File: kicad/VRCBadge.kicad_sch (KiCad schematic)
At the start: 34 parts, among them J4 Conn_01x02, J5 USB_C_Receptacle_USB2.0_16P, J6 Conn_01x13_Socket, Q2 FS8205A, SW3 RESET, SW4 BOOT, U10 MAX17048G+T10, U6 DW01A, U7 ME6211C33M5, U8 TP4056-42-ESOP8, U9 ESP32-S3-WROOM-1U

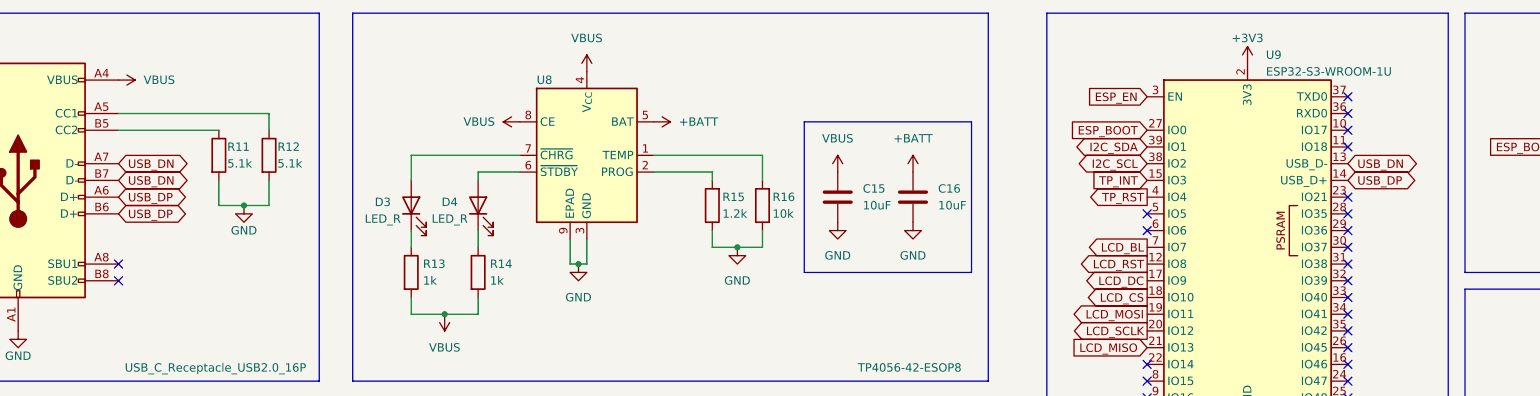
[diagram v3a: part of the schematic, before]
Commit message: chore: change usb data line global label and update footprint to 0402_1005
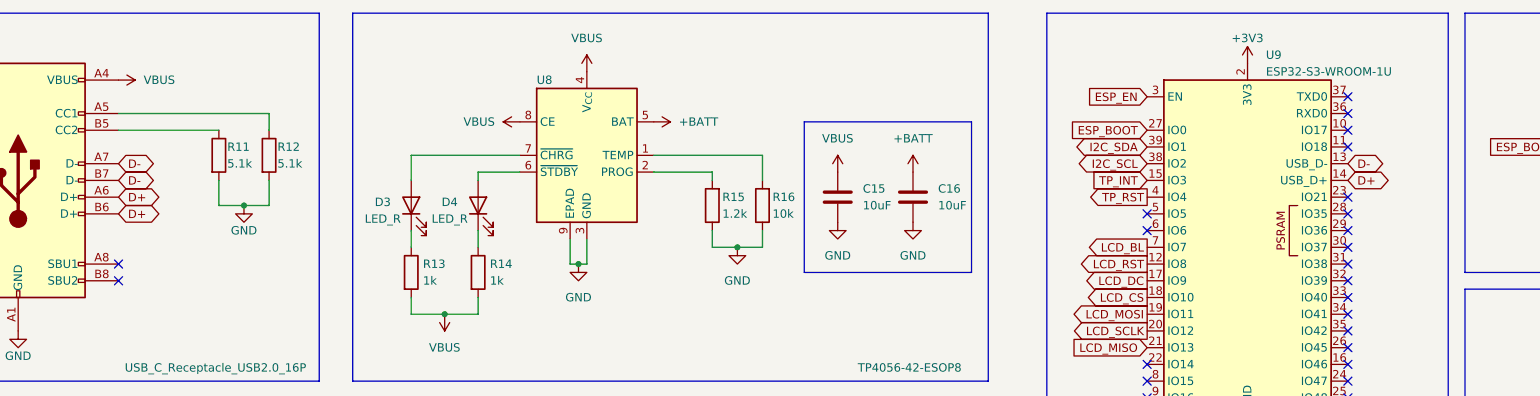
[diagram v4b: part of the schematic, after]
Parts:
- C12, C13, C14, C17, C19, C20, C21, C22: footprint Capacitor_SMD:C_0603_1608Metric -> Capacitor_SMD:C_0402_1005Metric
- C15, C16, C18: footprint Capacitor_SMD:C_0805_2012Metric -> Capacitor_SMD:C_0402_1005Metric
- D3, D4: footprint LED_SMD:LED_0603_1608Metric -> LED_SMD:LED_0402_1005Metric
- R11, R12, R13, R14, R15, R16, R17, R18, R19, R20: footprint Resistor_SMD:R_0603_1608Metric -> Resistor_SMD:R_0402_1005Metric
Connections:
- net USB_DN renamed D-
- net USB_DP renamed D+
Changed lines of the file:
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@@
 		)
 	)
-	(global_label "USB_DP"
+	(global_label "D+"
 		(shape bidirectional)
 		(at 50.8 48.26 0)
@@
 		)
 		(property "Intersheetrefs" "${INTERSHEET_REFS}"
-			(at 62.2141 48.26 0)
+			(at 57.7389 48.26 0)
 			(effects
 				(font
@@
 		)
 	)
-	(global_label "USB_DP"
+	(global_label "D+"
 		(shape bidirectional)
 		(at 50.8 50.8 0)
@@
 		)
 		(property "Intersheetrefs" "${INTERSHEET_REFS}"
-			(at 62.2141 50.8 0)
+			(at 57.7389 50.8 0)
 			(effects
 				(font
@@
 		)
 	)
-	(global_label "USB_DN"
+	(global_label "D-"
 		(shape bidirectional)
 		(at 50.8 43.18 0)
@@
 		)
 		(property "Intersheetrefs" "${INTERSHEET_REFS}"
-			(at 62.2746 43.18 0)
+			(at 57.7389 43.18 0)
 			(effects
 				(font
@@
 		)
 	)
-	(global_label "USB_DN"
+	(global_label "D-"
 		(shape bidirectional)
 		(at 237.49 43.18 0)
@@
 		)
 		(property "Intersheetrefs" "${INTERSHEET_REFS}"
-			(at 248.9646 43.18 0)
+			(at 244.4289 43.18 0)
 			(effects
 				(font
@@
 		)
 	)
-	(global_label "USB_DP"
+	(global_label "D+"
 		(shape bidirectional)
 		(at 237.49 45.72 0)
@@
 		)
 		(property "Intersheetrefs" "${INTERSHEET_REFS}"
-			(at 248.9041 45.72 0)
+			(at 244.4289 45.72 0)
 			(effects
 				(font
@@
 		)
 	)
-	(global_label "USB_DN"
+	(global_label "D-"
 		(shape bidirectional)
 		(at 50.8 45.72 0)
@@
 		)
 		(property "Intersheetrefs" "${INTERSHEET_REFS}"
-			(at 62.2746 45.72 0)
+			(at 57.7389 45.72 0)
 			(effects
 				(font
@@
 			)
 		)
-		(property "Footprint" "Resistor_SMD:R_0603_1608Metric"
+		(property "Footprint" "Resistor_SMD:R_0402_1005Metric"
 			(at 308.102 31.75 90)
 			(effects
@@
 			)
 		)
-		(property "Footprint" "Resistor_SMD:R_0603_1608Metric"
+		(property "Footprint" "Resistor_SMD:R_0402_1005Metric"
 			(at 64.262 41.91 90)
 			(effects
@@
 			)
 		)
-		(property "Footprint" "LED_SMD:LED_0603_1608Metric"
+		(property "Footprint" "LED_SMD:LED_0402_1005Metric"
 			(at 105.41 49.53 0)
 			(effects
@@
 			)
 		)
-		(property "Footprint" "LED_SMD:LED_0603_1608Metric"
+		(property "Footprint" "LED_SMD:LED_0402_1005Metric"
 			(at 95.25 49.53 0)
 			(effects
@@
 			)
 		)
-		(property "Footprint" "Capacitor_SMD:C_0805_2012Metric"
+		(property "Footprint" "Capacitor_SMD:C_0402_1005Metric"
 			(at 262.5852 120.65 0)
 			(effects
@@
 			)
 		)
-		(property "Footprint" "Resistor_SMD:R_0603_1608Metric"
+		(property "Footprint" "Resistor_SMD:R_0402_1005Metric"
 			(at 316.992 31.75 90)
 			(effects
@@
 			)
 		)
-		(property "Footprint" "Capacitor_SMD:C_0603_1608Metric"
+		(property "Footprint" "Capacitor_SMD:C_0402_1005Metric"
 			(at 275.2852 93.98 0)
 			(effects
@@
 			)
 		)
-		(property "Footprint" "Capacitor_SMD:C_0603_1608Metric"
+		(property "Footprint" "Capacitor_SMD:C_0402_1005Metric"
 			(at 145.7452 101.6 0)
 			(effects
@@
 			)
 		)
-		(property "Footprint" "Capacitor_SMD:C_0603_1608Metric"
+		(property "Footprint" "Capacitor_SMD:C_0402_1005Metric"
 			(at 236.22 163.5252 0)
 			(effects
@@
 			)
 		)
-		(property "Footprint" "Resistor_SMD:R_0603_1608Metric"
+		(property "Footprint" "Resistor_SMD:R_0402_1005Metric"
 			(at 142.748 49.53 90)
 			(effects
@@
 			)
 		)
-		(property "Footprint" "Resistor_SMD:R_0603_1608Metric"
+		(property "Footprint" "Resistor_SMD:R_0402_1005Metric"
 			(at 71.882 41.91 90)
 			(effects
@@
 			)
 		)
-		(property "Footprint" "Capacitor_SMD:C_0603_1608Metric"
+		(property "Footprint" "Capacitor_SMD:C_0402_1005Metric"
 			(at 256.2352 153.67 0)
 			(effects
@@
 			)
 		)
-		(property "Footprint" "Resistor_SMD:R_0603_1608Metric"
+		(property "Footprint" "Resistor_SMD:R_0402_1005Metric"
 			(at 275.082 33.02 90)
 			(effects
@@
 			)
 		)
-		(property "Footprint" "Capacitor_SMD:C_0603_1608Metric"
+		(property "Footprint" "Capacitor_SMD:C_0402_1005Metric"
 			(at 287.9852 120.65 0)
 			(effects
@@
 			)
 		)
-		(property "Footprint" "Resistor_SMD:R_0603_1608Metric"
+		(property "Footprint" "Resistor_SMD:R_0402_1005Metric"
 			(at 272.542 74.93 90)
 			(effects
@@
 			)
 		)
-		(property "Footprint" "Capacitor_SMD:C_0805_2012Metric"
+		(property "Footprint" "Capacitor_SMD:C_0402_1005Metric"
 			(at 160.9852 52.07 0)
 			(effects
@@
 			)
 		)
-		(property "Footprint" "Resistor_SMD:R_0603_1608Metric"
+		(property "Footprint" "Resistor_SMD:R_0402_1005Metric"
 			(at 93.472 59.69 90)
 			(effects
@@
 			)
 		)
-		(property "Footprint" "Capacitor_SMD:C_0603_1608Metric"
+		(property "Footprint" "Capacitor_SMD:C_0402_1005Metric"
 			(at 134.3152 101.6 0)
 			(effects
@@
 			)
 		)
-		(property "Footprint" "Capacitor_SMD:C_0603_1608Metric"
+		(property "Footprint" "Capacitor_SMD:C_0402_1005Metric"
 			(at 69.5452 137.16 0)
 			(effects
@@
 			)
 		)
-		(property "Footprint" "Capacitor_SMD:C_0603_1608Metric"
+		(property "Footprint" "Capacitor_SMD:C_0402_1005Metric"
 			(at 275.2852 120.65 0)
 			(effects
@@
 			)
 		)
-		(property "Footprint" "Resistor_SMD:R_0603_1608Metric"
+		(property "Footprint" "Resistor_SMD:R_0402_1005Metric"
 			(at 150.368 49.53 90)
 			(effects
@@
 			)
 		)
-		(property "Footprint" "Resistor_SMD:R_0603_1608Metric"
+		(property "Footprint" "Resistor_SMD:R_0402_1005Metric"
 			(at 103.632 59.69 90)
 			(effects
@@
 			)
 		)
-		(property "Footprint" "Capacitor_SMD:C_0805_2012Metric"
+		(property "Footprint" "Capacitor_SMD:C_0402_1005Metric"
 			(at 172.4152 52.07 0)
 			(effects
